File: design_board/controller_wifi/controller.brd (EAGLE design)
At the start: 123.2 x 84 mm, 58 parts, among them IC1 L293D, IC2 7805DT, IC4 7805TV

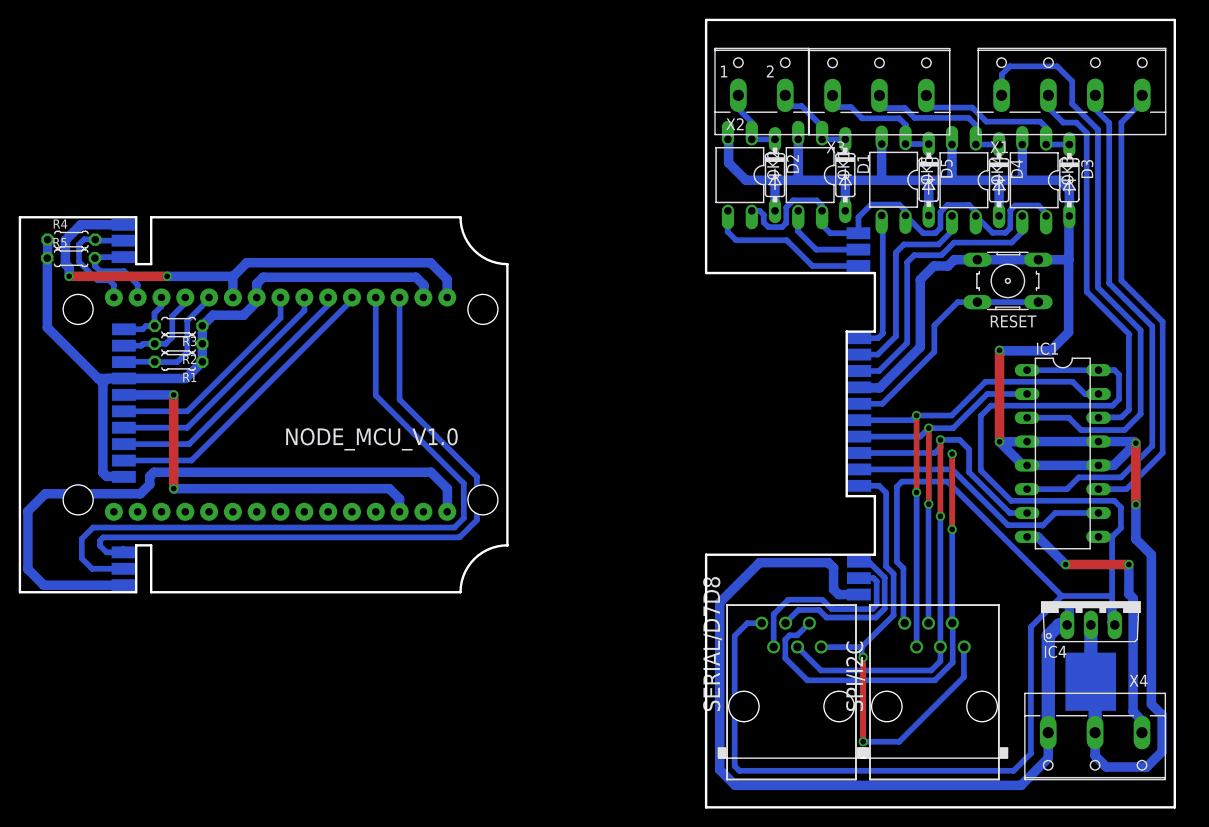
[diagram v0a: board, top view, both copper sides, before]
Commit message: Изменен модуль контроллера с wifi (добавлены конденсаторы на линии питания, резисторы на входе  - перед оптопарами)
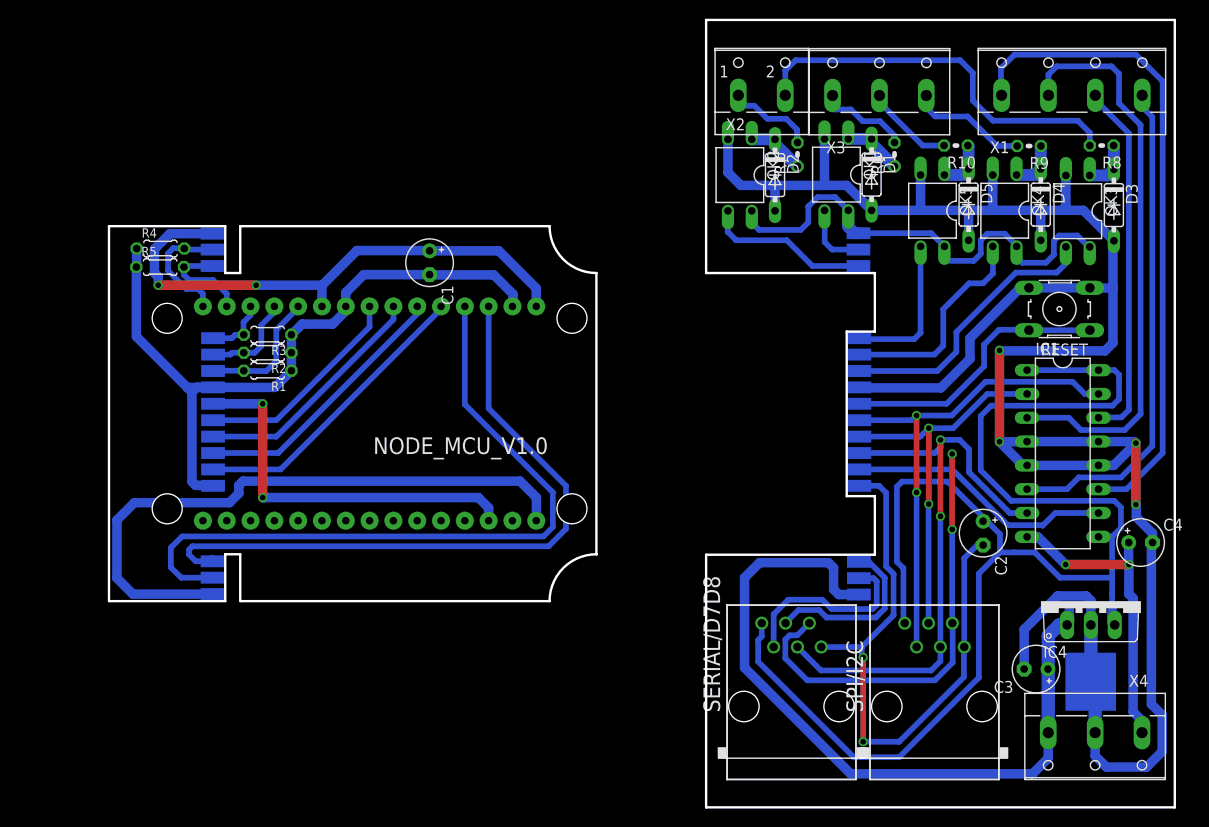
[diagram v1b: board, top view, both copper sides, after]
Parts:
- added C1, C2, C3, C4: (no value), resistor:E2,5-5
- added R10, R6, R7, R8, R9: (no value), resistor:0204V
- moved NODE_MCU_V1.0 9.55 mm to (-34.6, 58.3)
- moved PAD1 9.55 mm to (-51.4, 39.0)
- moved PAD10 9.55 mm to (-51.4, 55.8)
- moved PAD11 9.55 mm to (-51.4, 54.0)
- moved PAD12 9.55 mm to (-51.4, 52.3)
- moved PAD13 9.55 mm to (-51.4, 77.5)
- moved PAD2 9.55 mm to (-51.4, 50.5)
- moved PAD20 9.55 mm to (-51.4, 61.0)
- moved PAD21 9.55 mm to (-51.4, 42.5)
- moved PAD22 9.55 mm to (-51.4, 40.8)
- moved PAD3 9.55 mm to (-51.4, 59.3)
- moved PAD4 9.55 mm to (-51.4, 62.8)
- moved PAD5 9.55 mm to (-51.4, 64.5)
- moved PAD6 9.55 mm to (-51.4, 66.3)
- moved PAD7 9.55 mm to (-51.4, 75.8)
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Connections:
- new net N$10: R8.2, X2.2
- new net N$23: R7.2, X2.1
- new net N$24: R9.2, X3.3
- new net N$25: R10.2, X3.2
- new net N$26: R6.2, X3.1
- net +12V: now also C3.+
- net +3V3: now also C1.+
- net +5V: now also C2.+
- net GND: now also C1.-, C2.-, C3.-, C4.-
- net N$1: now also R9.1; no longer X3.2
- net N$11: now also R10.1; no longer X3.1
- net N$12: now also X1.4; no longer X1.3
- net N$14: now also X1.2; no longer X1.1
- net N$20: now also X1.1; no longer X1.4
- net N$21: now also X1.3; no longer X1.2
- net N$22: now also R6.1; no longer X2.2
- net N$7: now also R7.1; no longer X2.1
- net N$9: now also R8.1; no longer X3.3
- net VCC/2: now also C4.+
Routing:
- net N$10: track 0.00 -> 41.9 mm
- net GND: track 355.7 -> 388.1 mm
- net N$20: track 49.3 -> 70.0 mm
- net +5V: track 177.8 -> 160.4 mm
- net N$9: track 19.1 -> 5.40 mm
- net N$1: track 18.3 -> 5.30 mm
- net N$24: track 0.00 -> 12.7 mm
- net +12V: track 160.1 -> 149.0 mm
- net N$26: track 0.00 -> 9.87 mm
- net N$23: track 0.00 -> 9.82 mm
- net N$25: track 0.00 -> 9.79 mm
- net N$11: track 15.1 -> 5.37 mm
- net +3V3: track 104.6 -> 110.3 mm
- net N$18: track 67.5 -> 70.5 mm
- net N$21: track 41.5 -> 39.1 mm
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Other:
- board size 123.2 x 84 mm -> 113.7 x 84 mm

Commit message: Изменен модуль контроллера с wifi (заменены разъемы RJ-11, увеличина толщина дорожек), добавлены используемые библиотеки.
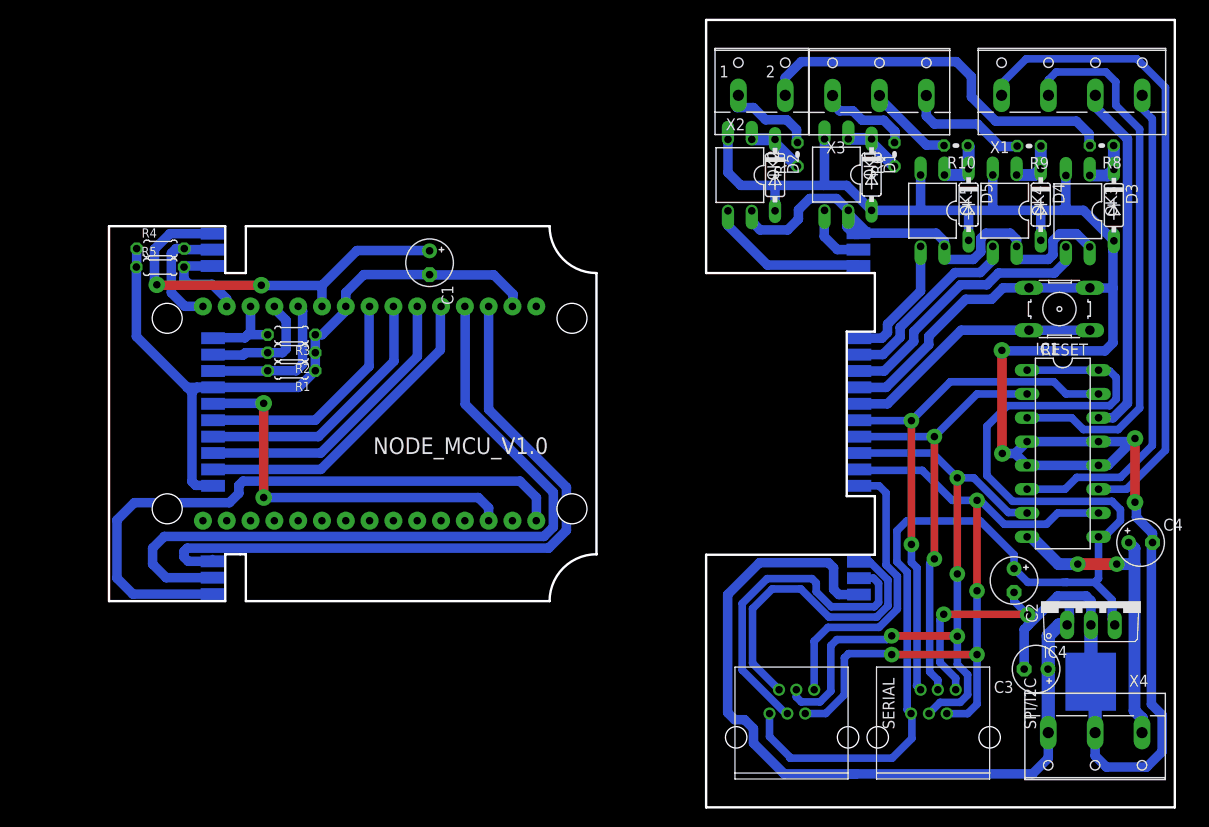
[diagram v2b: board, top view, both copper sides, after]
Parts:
- removed SERIAL/D7D8: RJ11-6X, con-tycoelectronics:RJ11-NO_SHIELD
- added SERIAL: RJ11, con-rj-11-6P6:RJ11
- SPI/I2C: value RJ11-6X -> RJ11; device con-tycoelectronics:RJ11-NO_SHIELD -> con-rj-11-6P6:RJ11
- moved C2 6.03 mm to (34.1, 40.5)
- moved SPI/I2C 4.78 mm to (27.1, 22.4), turned to 270 degrees
- moved R1 2.55 mm to (-43.0, 62.8)
- moved R2 2.55 mm to (-43.0, 64.8)
- moved R3 2.55 mm to (-43.0, 66.7)
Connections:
- net +5V: now also SERIAL.6, SPI/I2C.6; no longer SERIAL/D7D8.1, SPI/I2C.1
- net GND: now also SERIAL.1, SPI/I2C.1; no longer SERIAL/D7D8.6, SPI/I2C.6
- net N$13: now also SERIAL.3; no longer SERIAL/D7D8.4
- net N$15: now also SERIAL.2, SPI/I2C.2; no longer SERIAL/D7D8.5, SPI/I2C.5
- net N$16: now also SERIAL.5; no longer SERIAL/D7D8.3
- net N$19: now also SPI/I2C.5; no longer SPI/I2C.2
- net N$8: now also SERIAL.4; no longer SERIAL/D7D8.2
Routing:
- net +5V: track 160.4 -> 130.8 mm
- net N$8: track 96.4 -> 116.8 mm
- net N$16: track 90.7 -> 107.9 mm
- net +3V3: track 110.3 -> 98.5 mm
- net N$13: track 94.0 -> 105.0 mm, vias 2 -> 4
- net GND: track 388.1 -> 377.1 mm
- net N$17: track 66.6 -> 76.0 mm
- net N$19: track 75.5 -> 82.4 mm
- net +12V: track 149.0 -> 155.8 mm
- net N$15: track 109.2 -> 111.4 mm, vias 2 -> 4
- net N$14: track 61.0 -> 59.0 mm
- net N$2: track 43.8 -> 45.3 mm
- net N$20: track 70.0 -> 68.7 mm
- net N$18: track 70.5 -> 69.2 mm
- net N$10: track 41.9 -> 40.7 mm
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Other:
- outline, holes or cut-outs redrawn
